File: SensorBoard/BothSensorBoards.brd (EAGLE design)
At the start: 37.8 x 19.5 mm, 33 parts, among them IC1 MEGA8-AI, IC2 SN65176D, IC3 LM2936M-3.3, IC4 LM2936M-5.0

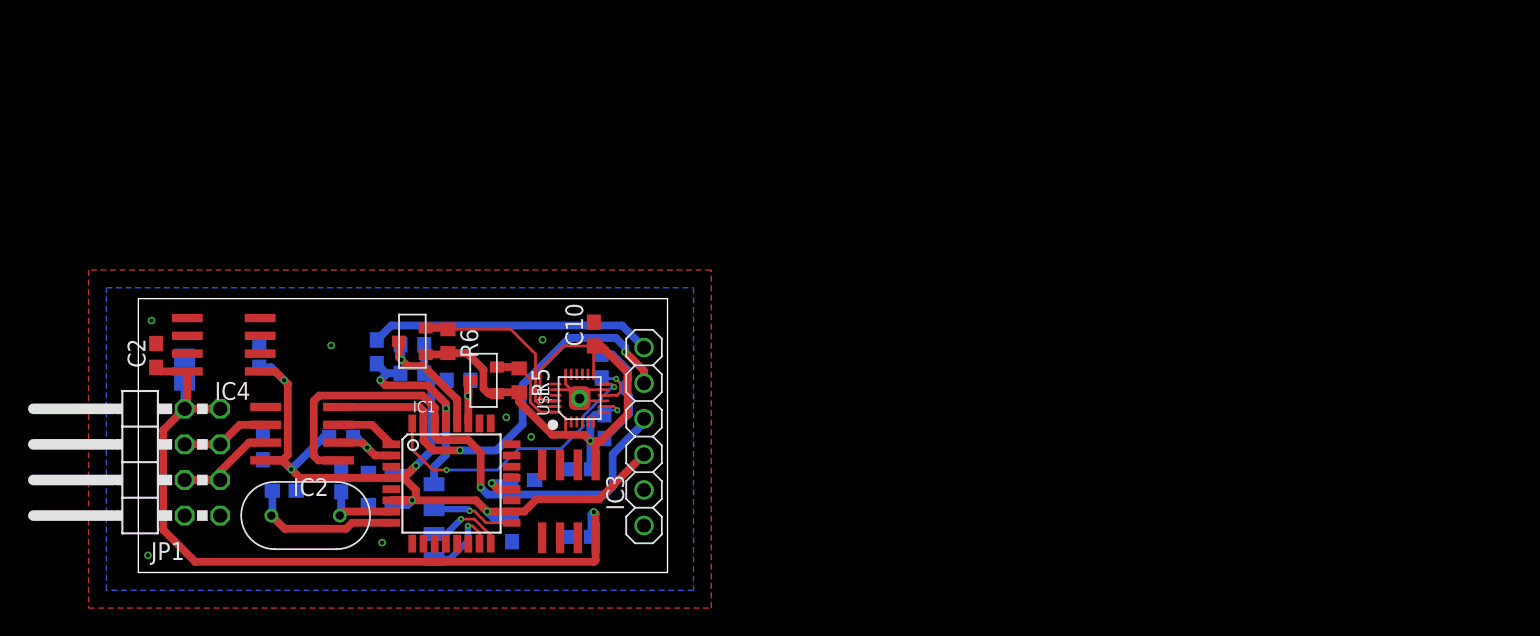
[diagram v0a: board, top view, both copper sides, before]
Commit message: added pads for flashing the bootloader to sensor board, added alternative version of sensor board
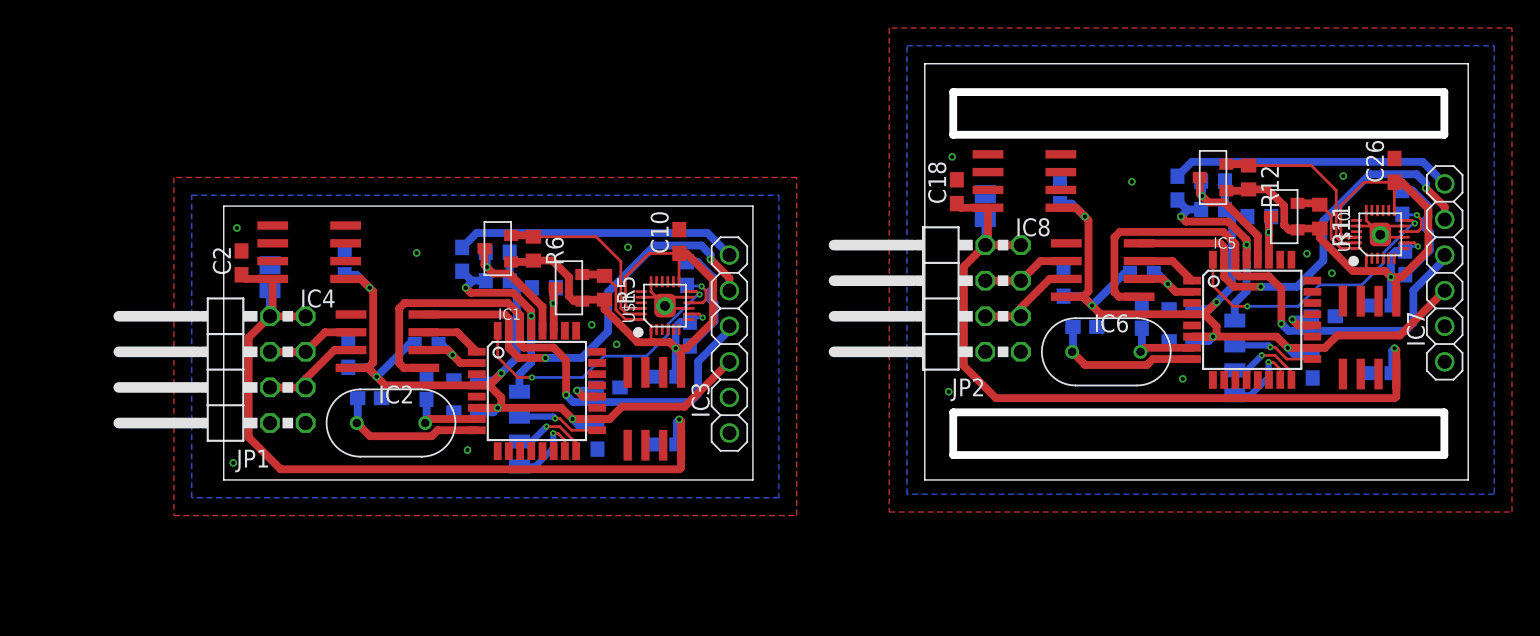
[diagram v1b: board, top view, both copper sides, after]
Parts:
- added C17: 10u, resistor:C0805
- added C18, C22: 330n, resistor:C0603
- added C19, C24, C25, C26, C27, C28, C29, C30, C31, C32: 100n, resistor:C0603
- added C20: 10n, resistor:C0603
- added C21, C23: 56p, resistor:C0603
- added IC5: MEGA8-AI, atmel:TQFP32-08
- added IC6: SN65176D, texas:SO-08
- added IC7: LM2936M-3.3, national-semiconductor:SO08
- added IC8: LM2936M-5.0, national-semiconductor:SO08
- added JP2: (no value), pinhead:2X04/90
- added R10, R11, R12, R7, R8, R9: 10k, resistor:R0603
- added U$10: MPU-9250, invensense:LEAD-QFN24
- added U$11: FTDI-PINHEADER, FTDI-PINHEADER:FTDI-PINHEADER
- added U$12: ISP_PADS, ISP_Pads:ISP_PADS
- added U$7, U$8: 2N7002E, 2N7002E:SOT-23-3
- added U$9: LFXTAL003240BULK, LFXTAL003240Bulk:LFXTAL003240BULK
- moved C11 8.99 mm to (39.2, 21.3)
- moved C1 8.99 mm to (9.40, 21.1)
- moved C12 8.99 mm to (33.5, 13.2)
- moved C14 8.99 mm to (37.6, 14.0)
- moved C15 8.99 mm to (23.1, 22.4)
- moved C5 8.99 mm to (20.6, 13.2)
- moved C6 8.99 mm to (37.6, 9.14)
- moved C7 8.99 mm to (16.5, 12.4)
- moved C8 8.99 mm to (23.4, 11.4)
- moved IC1 8.99 mm to (28.4, 13.0)
- moved IC2 8.99 mm to (17.8, 16.5)
- moved JP1 8.99 mm to (5.59, 14.5)
- moved R1 8.99 mm to (20.6, 16.3)
- moved R4 8.99 mm to (29.0, 20.3)
- moved R5 8.99 mm to (33.3, 20.3)
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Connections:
- new net +3V1: C20.1, C26.1, C30.1, IC7.1, R11.2, R12.2, U$10.1, U$10.13, U$10.22, U$10.8, U$7.P$1, U$8.P$1
- new net +5V1: C19.1, C24.1, C25.1, C29.1, C32.1, IC5.18, IC5.4, IC5.6, IC6.8, IC8.1, R10.2, R7.2, R8.2, R9.2, U$11.P$3
- new net -RE1: IC5.2, IC6.2, R7.1
- new net /RESET1: C31.2, IC5.29, R8.1, U$12.P$4
- new net DE1: IC5.1, IC6.3
- new net DTR1: C31.1, U$11.P$6
- new net GND1: C17.2, C18.2, C19.2, C20.2, C21.2, C22.2, C23.2, C24.2, C25.2, C26.2, C27.2, C28.2, C29.2, C30.2, C32.2, IC5.21, IC5.3, IC5.5, IC6.5, IC7.2, IC7.3, IC7.6, IC7.7, IC8.2, IC8.3, IC8.6, IC8.7, JP2.1, JP2.2, U$10.11, U$10.18, U$10.20, U$10.25, U$10.9, U$11.P$1, U$11.P$2
- new net INT1: IC5.32, U$10.12
- new net MISO1: IC5.16, U$12.P$2
- new net MOSI1: IC5.15, U$12.P$1
- new net N$10: R11.1, U$10.24, U$8.P$2
- new net N$11: C27.1, U$10.10
- new net N$12: C21.1, IC5.7, U$9.P$1
- new net N$13: C23.1, IC5.8, U$9.P$2
- new net N$14: C28.1, IC5.20
- new net N$15: IC6.6, JP2.5, JP2.6
- new net N$16: IC6.7, JP2.3, JP2.4
- new net N$8: R12.1, U$10.23, U$7.P$2
- new net RX1: IC5.30, IC6.1, U$11.P$4
- new net SCK1: IC5.17, U$12.P$3
- new net SCL1: IC5.28, R9.1, U$7.P$3
- new net SDA1: IC5.27, R10.1, U$8.P$3
- new net TX1: IC5.31, IC6.4, U$11.P$5
- new net VCC1: C17.1, C18.1, C22.1, IC7.8, IC8.8, JP2.7, JP2.8
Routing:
- net +5V1: track 0.00 -> 67.2 mm, vias 0 -> 5
- net VCC1: track 0.00 -> 56.0 mm, vias 0 -> 1
- net +3V1: track 0.00 -> 45.5 mm, vias 0 -> 2
- net RX1: track 0.00 -> 38.9 mm, vias 0 -> 1
- net TX1: track 0.00 -> 31.4 mm, vias 0 -> 2
- net INT1: track 0.00 -> 20.6 mm, vias 0 -> 2
- net DTR1: track 0.00 -> 20.2 mm
- net GND1: track 0.00 -> 15.9 mm, vias 0 -> 8
- net /RESET1: track 0.00 -> 15.2 mm, vias 0 -> 2
- net N$8: track 0.00 -> 13.6 mm
- net N$13: track 0.00 -> 10.9 mm
- net SCL1: track 0.00 -> 9.35 mm, vias 0 -> 1
- net N$16: track 0.00 -> 7.24 mm
- net N$10: track 0.00 -> 6.51 mm
- net N$15: track 0.00 -> 6.36 mm
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- added copper zone on layer 1, net GND1
- added copper zone on layer 16, net GND1
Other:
- board size 37.8 x 19.5 mm -> 88.8 x 29.7 mm
